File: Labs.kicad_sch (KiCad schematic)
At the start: 34 parts, among them J1 PROG_port, SW1BOOT1 SW_Push, SW2NRST1 SW_Push, U1 STM32F407VGTx, Y1 Crystal

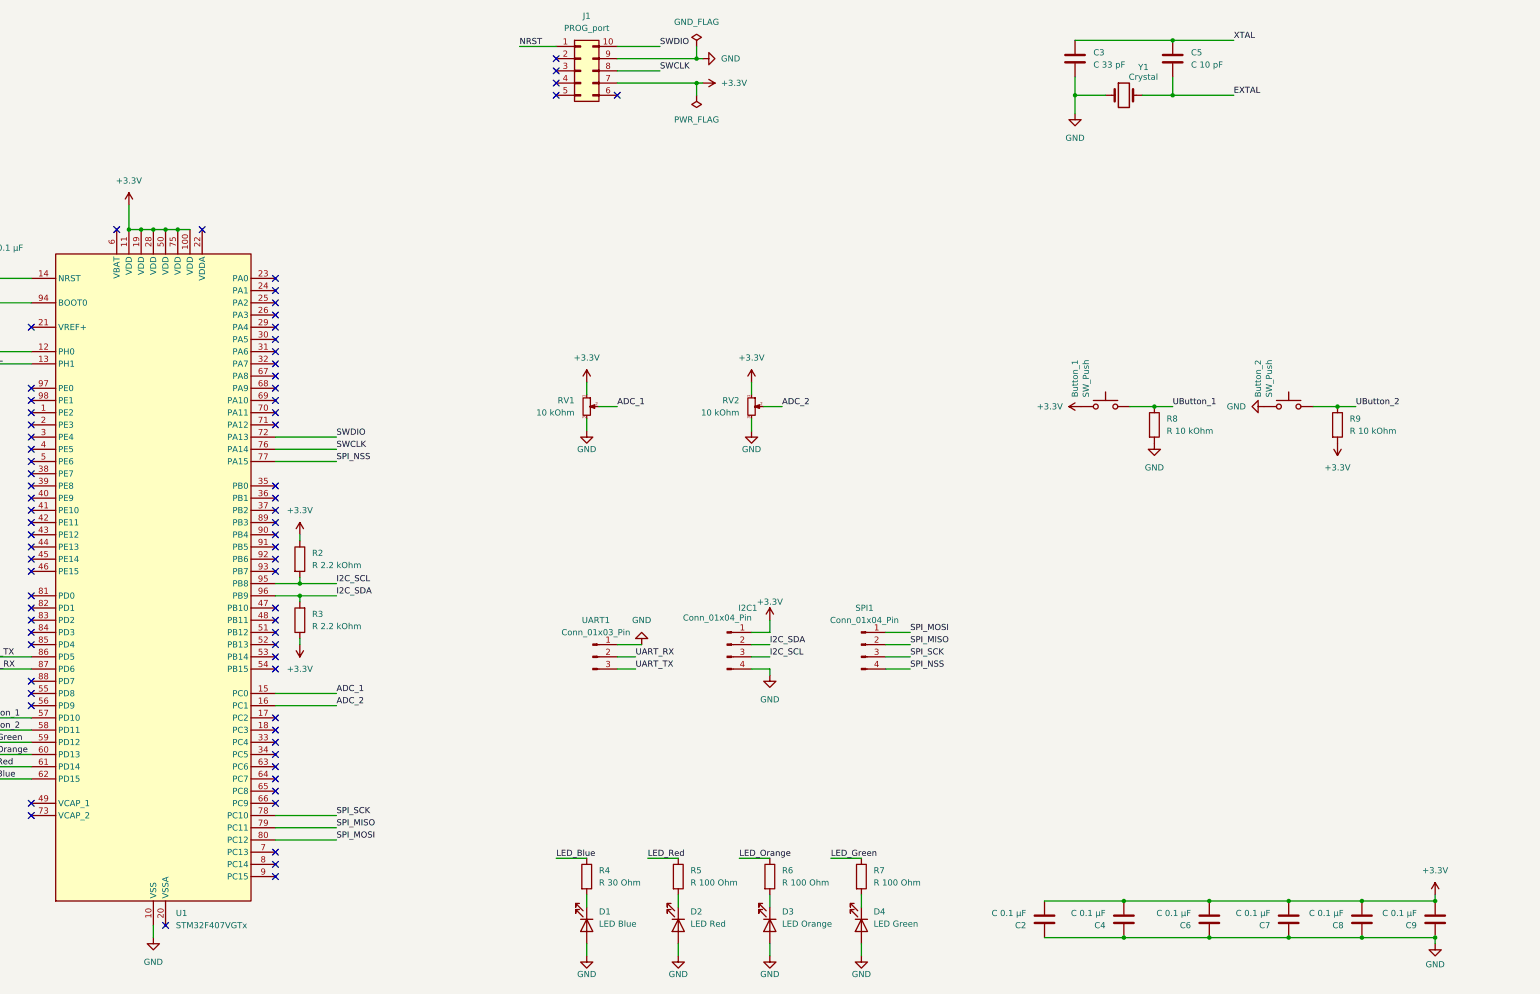
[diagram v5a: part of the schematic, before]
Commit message: feat: add pwr supply from type-c connector
feat: add pwr supply from bat

feat: add dc/dc lower pwr

feat: add pwr for extern sensors

fix: replace adc to another pin
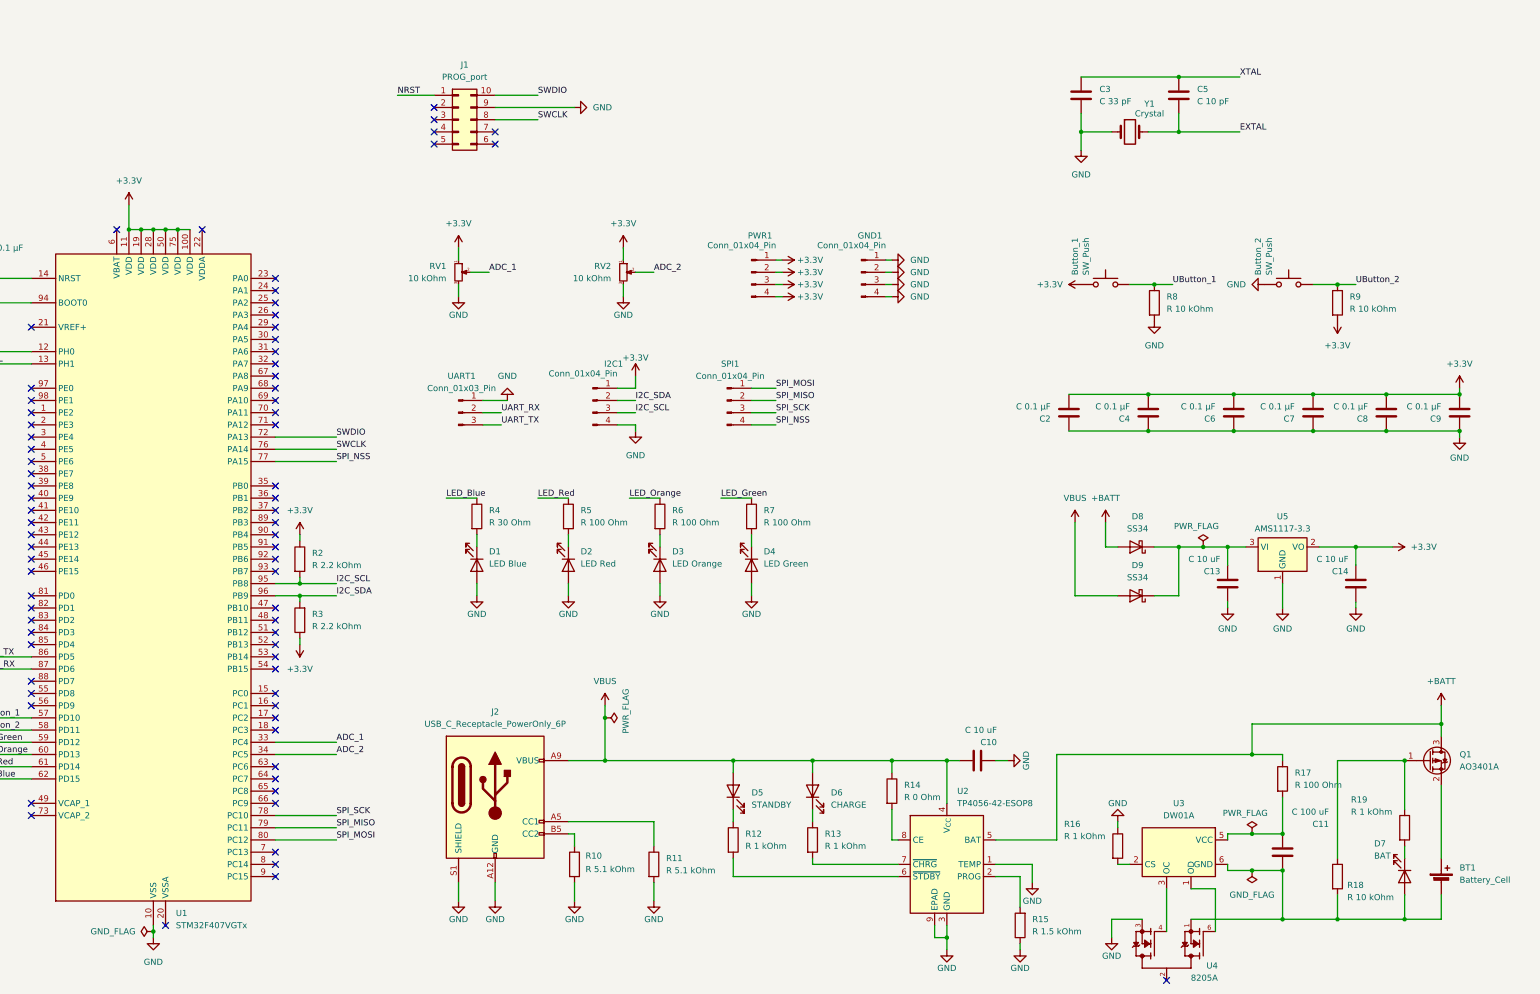
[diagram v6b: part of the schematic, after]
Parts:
- added BT1: Battery_Cell, Battery:BatteryHolder_MPD_BH-18650-PC, symbol Device:Battery_Cell
- added C10, C13, C14: C 10 uF, Capacitor_SMD:C_0805_2012Metric_Pad1.18x1.45mm_HandSolder, symbol Device:C
- added C11: C 100 uF, Capacitor_SMD:C_0805_2012Metric_Pad1.18x1.45mm_HandSolder, symbol Device:C
- added D5: STANDBY, LED_SMD:LED_0805_2012Metric, symbol Device:LED
- added D6: CHARGE, LED_SMD:LED_0805_2012Metric, symbol Device:LED
- added D7: BAT, LED_SMD:LED_0805_2012Metric, symbol Device:LED
- added D8, D9: SS34, Diode_SMD:D_SMA, symbol Diode:SS34
- added GND1, PWR1: Conn_01x04_Pin, Connector_PinHeader_2.54mm:PinHeader_1x04_P2.54mm_Horizontal, symbol Connector:Conn_01x04_Pin
- added J2: USB_C_Receptacle_PowerOnly_6P, Connector_USB:USB_C_Receptacle_GCT_USB4125-xx-x-0190_6P_TopMnt_Horizontal, symbol Connector:USB_C_Receptacle_PowerOnly_6P
- added Q1: AO3401A, Package_TO_SOT_SMD:SOT-23, symbol Transistor_FET:AO3401A
- added R10, R11: R 5.1 kOhm, Resistor_SMD:R_0805_2012Metric_Pad1.20x1.40mm_HandSolder, symbol Device:R
- added R12, R13, R16, R19: R 1 kOhm, Resistor_SMD:R_0805_2012Metric_Pad1.20x1.40mm_HandSolder, symbol Device:R
- added R14: R 0 Ohm, Resistor_SMD:R_0805_2012Metric_Pad1.20x1.40mm_HandSolder, symbol Device:R
- added R15: R 1.5 kOhm, Resistor_SMD:R_0805_2012Metric_Pad1.20x1.40mm_HandSolder, symbol Device:R
- added R17: R 100 Ohm, Resistor_SMD:R_0805_2012Metric_Pad1.20x1.40mm_HandSolder, symbol Device:R
- added R18: R 10 kOhm, Resistor_SMD:R_0805_2012Metric_Pad1.20x1.40mm_HandSolder, symbol Device:R
- added U2: TP4056-42-ESOP8, Package_SO:SOIC-8-1EP_3.9x4.9mm_P1.27mm_EP2.41x3.3mm_ThermalVias, symbol Battery_Management:TP4056-42-ESOP8
- added U3: DW01A, Package_TO_SOT_SMD:SOT-23-6, symbol Battery_Management:DW01A
- added U4: 8205A, 8205A:SOT95P285X140-6N, symbol 8205A:8205A
- added U5: AMS1117-3.3, Package_TO_SOT_SMD:SOT-223-3_TabPin2, symbol Regulator_Linear:AMS1117-3.3
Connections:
- net +3.3V: now also C14.2, PWR1.1 (Pin_1), PWR1.2 (Pin_2), PWR1.3 (Pin_3), PWR1.4 (Pin_4), U5.2 (VO); no longer J1.7 (Pin_7)
- net ADC_1: now also U1.33 (PC4); no longer U1.15 (PC0)
- net ADC_2: now also U1.34 (PC5); no longer U1.16 (PC1)
- net GND: now also C10.2, C13.1, C14.1, GND1.1 (Pin_1), GND1.2 (Pin_2), GND1.3 (Pin_3), GND1.4 (Pin_4), J2.A12 (GND), J2.B12 (GND), J2.S1 (SHIELD), R10.2, R11.2, R15.1, R16.1, U2.1 (TEMP), U2.3 (GND), U2.9 (EPAD), U4.3, U5.1 (GND)
- new net: Q1.1 (G), R18.1, R19.1
- new net: BT1.2 (-), C11.1, D7.2 (A), R18.2, U3.6 (GND), U4.1
- new net: R15.2, U2.2 (PROG)
- new net: R12.2, U2.6 (~{STDBY})
- new net: R13.2, U2.7 (~{CHRG})
- new net: R14.2, U2.8 (CE)
- new net: C13.2, D8.1 (K), D9.1 (K), U5.3 (VI)
- new net: D6.1 (K), R13.1
- new net: BT1.1 (+), Q1.2 (S)
- new net: J2.B5 (CC2), R10.1
- new net: D7.1 (K), R19.2
- new net: J2.A5 (CC1), R11.1
- new net: D5.1 (K), R12.1
- new net: U3.1 (OD), U4.6
- new net: R16.2, U3.2 (CS)
- new net: U3.3 (OC), U4.4
- new net: C11.2, R17.2, U3.5 (VCC)
- new net: U4.2, U4.5
- new net +BATT: D8.2 (A), Q1.3 (D), R17.1, U2.5 (BAT)
- new net VBUS: C10.1, D5.2 (A), D6.2 (A), D9.2 (A), J2.A9 (VBUS), J2.B9 (VBUS), R14.1, U2.4 (V_{CC})
- no-connect marks 73 -> 75
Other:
- moved on the sheet: Button_1, Button_2, C2, C3, C4, C5, C6, C7, C8, C9, D1, D2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

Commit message: feat: add tracing
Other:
- moved on the sheet: BT1, C10, C11, D5, D6, D7, J2, Q1, R10, R11, R12, R13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

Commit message: fix: minor fixes
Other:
- moved on the sheet: BT1, C10, C11, C13, C14, D1, D2, D3, D4, D5, D6, D7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
